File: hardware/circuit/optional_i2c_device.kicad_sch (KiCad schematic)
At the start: 2 parts, among them U2 BMP581

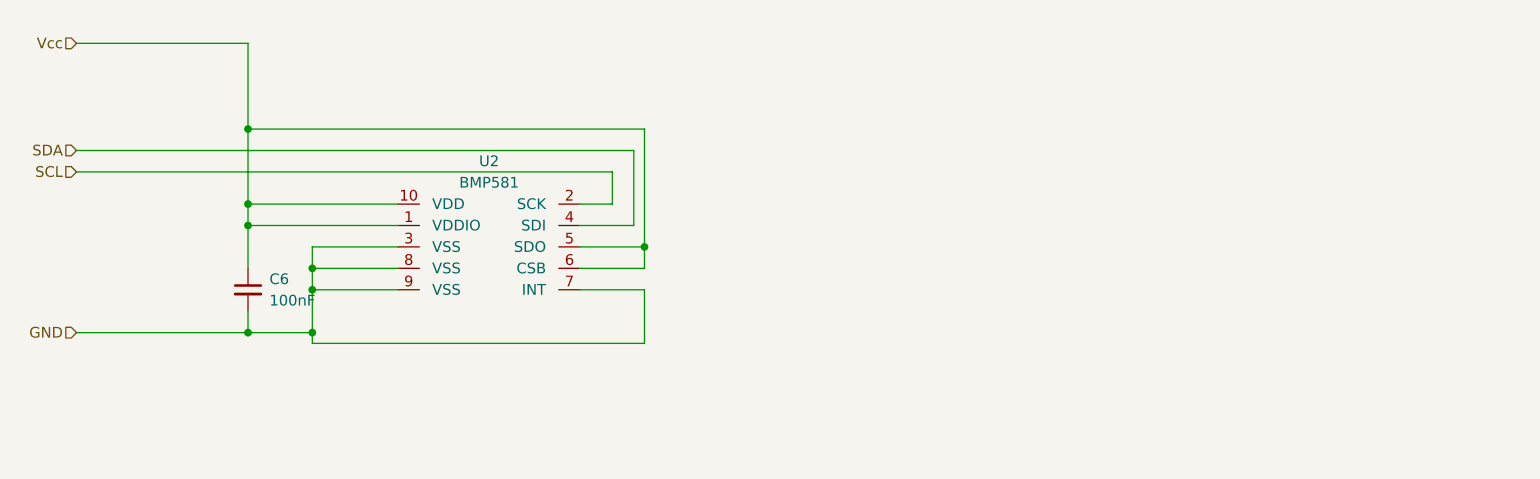
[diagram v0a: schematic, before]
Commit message: added optional i2c device, added gerber files - not tested! Use with care!
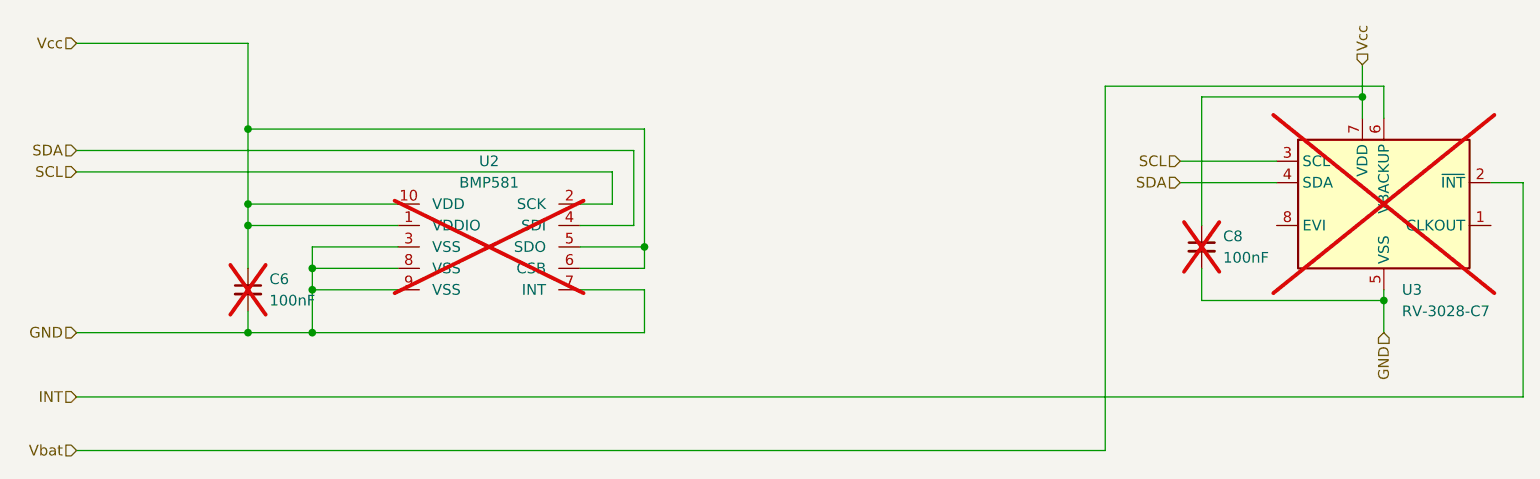
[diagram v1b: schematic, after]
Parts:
- added C8: 100nF, Capacitor_SMD:C_0805_2012Metric, symbol Device:C_Small
- added U3: RV-3028-C7, Package_SON:MicroCrystal_C7_SON-8_1.5x3.2mm_P0.9mm, symbol Timer_RTC:RV-3028-C7
- C6, U2: now not fitted
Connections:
- net GND: now also C8.2, U3.5 (VSS)
- net SCL: now also U3.3 (SCL)
- net SDA: now also U3.4 (SDA)
- net Vcc: now also C8.1, U3.7 (VDD)
- new net INT: U3.2 (~{INT})
- new net Vbat: U3.6 (VBACKUP)

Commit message: Update
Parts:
- removed C8: 100nF, Capacitor_SMD:C_0805_2012Metric, symbol Device:C_Small
- removed U3: RV-3028-C7, Package_SON:MicroCrystal_C7_SON-8_1.5x3.2mm_P0.9mm, symbol Timer_RTC:RV-3028-C7
- renumbered C6 to C7
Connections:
- net Vcc renamed 3V3
